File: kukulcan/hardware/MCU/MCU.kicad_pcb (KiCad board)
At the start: 4 copper layers, 78 x 53 mm, 88 parts, among them J1 Barrel_Jack_5V_In, J2 Barrel_Jack_5V_In, J3 USB_C_Receptacle, J4 SMA_GNSS, Q1 AO3401A, U1 TLV1117-33, U2 W25Q256JWEIQ, U3 ESP32-S3R16V, U4 BNO055, U5 NEO-M8N, U6 BMI088, U7 BME280, X1 40MHz, Y1 32.768kHz

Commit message: hw(mcu): update schematic and pcb
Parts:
- added svg2mod: G***, Core_System_2026:kukulcan, F.Cu at (163.5, 92.5)
- added svg2mod: G***, Core_System_2026:MarsRover, F.Cu at (141.2, 94.2)
- added svg2mod: G***, Core_System_2026:IMU_Axes_XYZ, F.Cu at (122.8, 87.2)
- FID1, FID2, FID3, FID4, FID5, FID6: footprint Fiducial:Fiducial_Cross_1.5mm_Mask2mm -> Fiducial:Fiducial_1mm_Mask3mm
- J4: footprint Connector_Coaxial:U.FL_Molex_MCRF_73412-0110_Vertical -> Connector_Coaxial:SMA_Amphenol_132134-10_Vertical
- U2: value W25Q256JWEIQ -> W25Q256JVEIQ; footprint Core_System_2026:W25Q256JWEIQ -> Core_System_2026:W25Q256JVEIQ
- U3: value ESP32-S3R16V -> ESP32-S3R8; footprint Core_System_2026:ESP32-S3R16V -> Core_System_2026:ESP32-S3R8
- moved FID6 59.0 mm to (125.8, 127.0)
- moved FID4 58.5 mm to (184.2, 82.0)
- moved FID5 45.0 mm to (184.2, 127.0)
- moved C29 4.25 mm to (125.5, 84.7), turned to 180 degrees
- moved J4 4.12 mm to (122.0, 119.0), turned to 90 degrees
- moved C28 3.55 mm to (125.8, 90.2), turned to 180 degrees
- moved C32 2.26 mm to (120.2, 111.8), turned to 180 degrees
- moved L3 1.68 mm to (119.2, 109.2), turned to -90 degrees
- moved U6 1.13 mm to (126.2, 87.5), turned to 180 degrees
- moved R14 0.79 mm to (120.2, 106.8)
- moved FID1 0.75 mm to (125.8, 81.2)
- moved FID3 0.50 mm to (184.2, 127.0)
- moved NxtPg1 0.25 mm to (150.0, 86.0)
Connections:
- net Net-(J4-In) renamed /RF_IN
- net Net-(L3-Pad1) renamed /RF2
- net Net-(U5-VCC_RF) renamed /RF1
- C5 pad 1: +VDD_SPI -> +3V3
- C6 pad 1: +VDD_SPI -> +3V3
- J3 pad S1: (no net) -> GND
- U2 pad 8: +VDD_SPI -> +3V3
- U3 pad 29: +VDD_SPI -> +3V3
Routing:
- net /RF_IN: track 0.00 -> 13.6 mm
- net +3V3: track 61.9 -> 71.5 mm, vias 48 -> 47
- net +VDD_SPI: track 9.01 -> 0.00 mm
- net SDA: track 74.3 -> 67.1 mm
- net GND: track 167.8 -> 174.0 mm, vias 124 -> 246
- net SCL: track 88.6 -> 94.2 mm
- net /RF1: track 0.00 -> 2.97 mm
- net NxtPg: track 16.4 -> 18.9 mm
- net /RF2: track 0.00 -> 1.66 mm
- net LED_WHITE: track 40.0 -> 41.0 mm
- net LedStrip: track 40.1 -> 40.9 mm
- net +VUSB: track 11.8 -> 12.4 mm
- removed copper zone on B.Cu, net +3V3
- removed copper zone on F.Cu, net +3V3
- removed copper zone on B.Cu, net +RB_VDD_5V
- removed copper zone on F.Cu, net +RB_VDD_5V
- removed copper zone on B.Cu, net +VDD_5V
- removed copper zone on F.Cu, net +VDD_5V
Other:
- board text added: "REV A RR 0126"

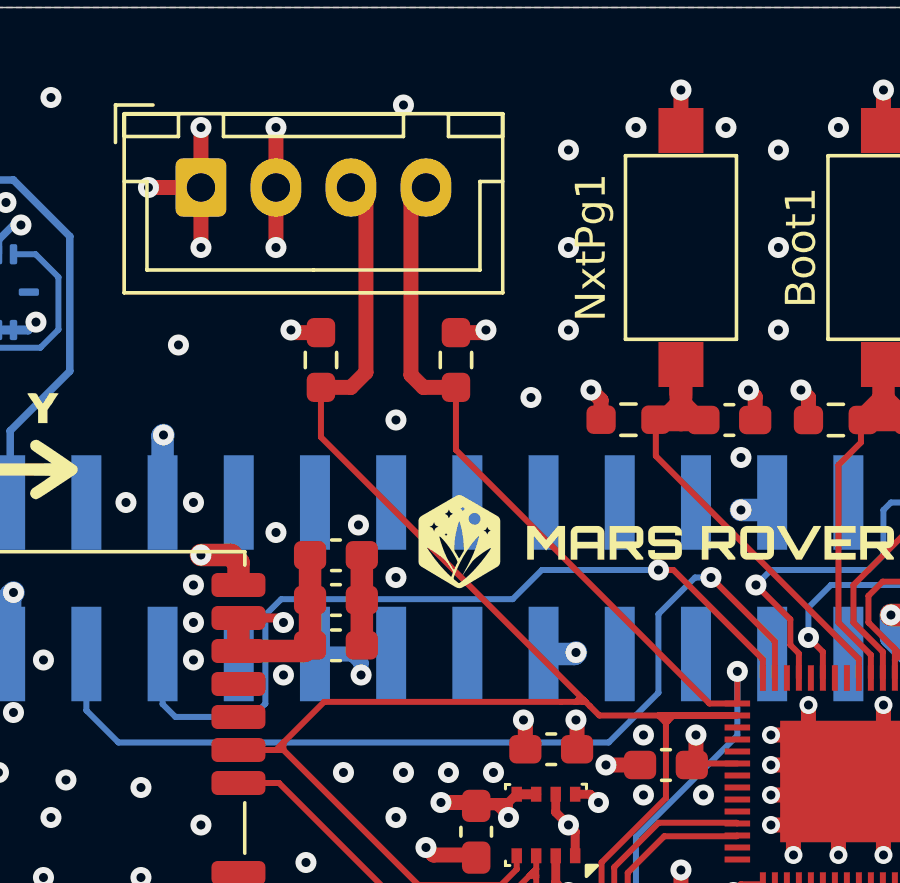
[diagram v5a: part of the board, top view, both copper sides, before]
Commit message: fix(kukulcan): I2C impedance change design error fix
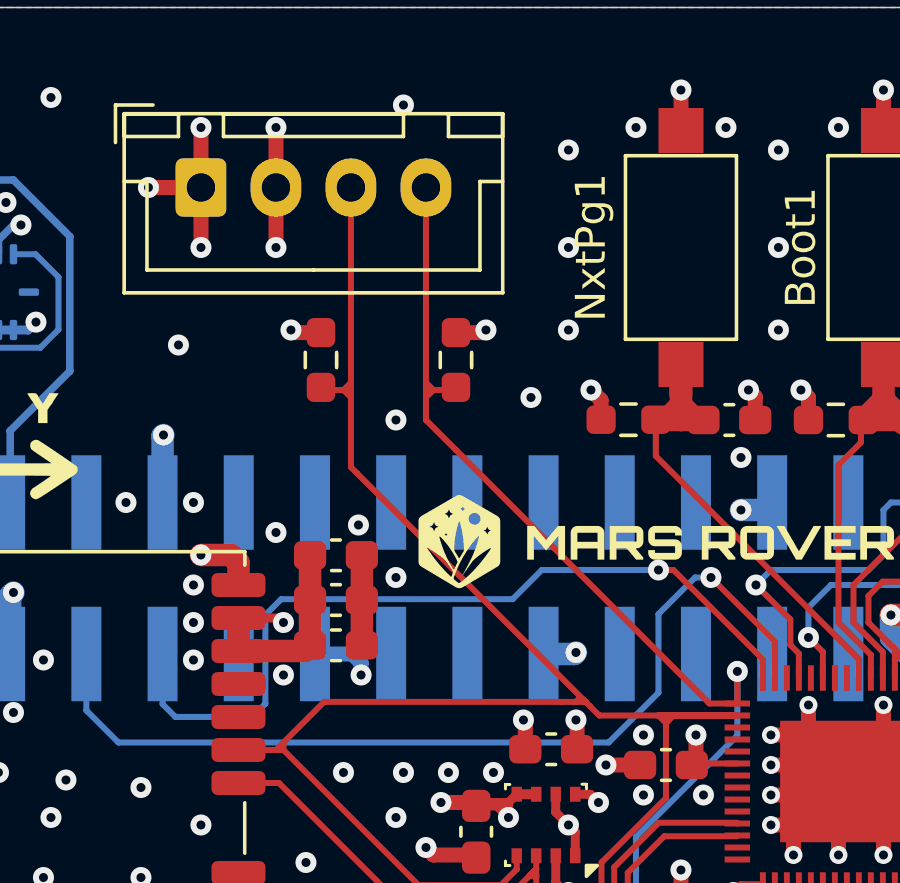
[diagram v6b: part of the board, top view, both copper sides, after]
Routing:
- net SDA: track 67.1 -> 67.8 mm
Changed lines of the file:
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@@
+	)
+	(segment
+		(start 139 90.5)
+		(end 139 84)
+		(width 0.2)
+		(layer "F.Cu")
+		(net 49)
 	)
 	(segment
@@
 	)
 	(segment
+		(start 139 90.75)
+		(end 139 90.5)
+		(width 0.2)
+		(layer "F.Cu")
+		(net 49)
+	)
+	(segment
 		(start 136.75 102.75)
 		(end 141.25 107.25)
@@
 	)
 	(segment
-		(start 138 92.322128)
-		(end 138 90.6625)
-		(width 0.2)
-		(layer "F.Cu")
-		(net 49)
-	)
-	(segment
-		(start 138 90.6625)
-		(end 139 90.6625)
-		(width 0.5)
+		(start 139 91)
+		(end 139 90.75)
+		(width 0.2)
 		(layer "F.Cu")
 		(net 49)
@@
 	)
 	(segment
+		(start 138.75 90.75)
+		(end 139 90.5)
+		(width 0.2)
+		(layer "F.Cu")
+		(net 49)
+	)
+	(segment
 		(start 146.752746 101.147)
 		(end 146.752746 101.074874)
@@
 	)
 	(segment
-		(start 139.5 90.1625)
-		(end 139.5 84.5)
-		(width 0.5)
-		(layer "F.Cu")
-		(net 49)
-	)
-	(segment
 		(start 141.775 114)
 		(end 142.5 114)
@@
 	)
 	(segment
+		(start 138.75 90.75)
+		(end 138.0875 90.75)
+		(width 0.2)
+		(layer "F.Cu")
+		(net 49)
+	)
+	(segment
+		(start 139 93.322128)
+		(end 139 91)
+		(width 0.2)
+		(layer "F.Cu")
+		(net 49)
+	)
+	(segment
+		(start 139 90.75)
+		(end 138.75 90.75)
+		(width 0.2)
+		(layer "F.Cu")
+		(net 49)
+	)
+	(segment
 		(start 149.5 102)
 		(end 149.5 101.85)
@@
 	(segment
 		(start 146.752746 101.074874)
-		(end 138 92.322128)
-		(width 0.2)
-		(layer "F.Cu")
-		(net 49)
-	)
-	(segment
-		(start 139.5 84.5)
-		(end 139 84)
-		(width 0.5)
+		(end 139.213936 93.536064)
+		(width 0.2)
 		(layer "F.Cu")
 		(net 49)
@@
 	)
 	(segment
+		(start 139.213936 93.536064)
+		(end 139 93.322128)
+		(width 0.2)
+		(layer "F.Cu")
+		(net 49)
+	)
+	(segment
 		(start 149.644 101.6)
 		(end 149.75 101.6)
@@
 	)
 	(segment
+		(start 138.0875 90.75)
+		(end 138 90.6625)
+		(width 0.2)
+		(layer "F.Cu")
+		(net 49)
+	)
+	(segment
 		(start 149.5 102)
 		(end 149.5 101.6)
@@
 	)
 	(segment
-		(start 139 90.6625)
-		(end 139.5 90.1625)
-		(width 0.5)
-		(layer "F.Cu")
-		(net 49)
-	)
-	(segment
 		(start 141.25 107.25)
 		(end 144 107.25)
@@
 		(start 146.752746 101.147)
 		(end 146.5 101.147)
+		(width 0.2)
+		(layer "F.Cu")
+		(net 49)
+	)
+	(segment
+		(start 139 91)
+		(end 138.75 90.75)
 		(width 0.2)
 		(layer "F.Cu")
@@
 	)
 	(segment
+		(start 141.5 91)
+		(end 141.5 90.75)
+		(width 0.2)
+		(layer "F.Cu")
+		(net 76)
+	)
+	(segment
 		(start 145.175 108)
 		(end 145.175 107)
@@
 	)
 	(segment
-		(start 142.5 92.75)
-		(end 142.5 90.6625)
+		(start 141.75 90.75)
+		(end 141.5 90.5)
+		(width 0.2)
+		(layer "F.Cu")
+		(net 76)
+	)
+	(segment
+		(start 141.5 90.75)
+		(end 141.75 90.75)
 		(width 0.2)
 		(layer "F.Cu")
@@
 	)
 	(segment
+		(start 142.4125 90.75)
+		(end 142.5 90.6625)
+		(width 0.2)
+		(layer "F.Cu")
+		(net 76)
+	)
+	(segment
 		(start 142.265271 113.0875)
 		(end 145.175 110.177771)
@@
 	)
 	(segment
-		(start 141 90.25)
-		(end 141 84.5)
-		(width 0.5)
-		(layer "F.Cu")
-		(net 76)
-	)
-	(segment
 		(start 145.175 108.575)
 		(end 145.25 108.5)
@@
 	)
 	(segment
+		(start 141.75 90.75)
+		(end 142.4125 90.75)
+		(width 0.2)
+		(layer "F.Cu")
+		(net 76)
+	)
+	(segment
+		(start 141.5 90.5)
+		(end 141.5 84)
+		(width 0.2)
+		(layer "F.Cu")
+		(net 76)
+	)
+	(segment
+		(start 141.5 91.75)
+		(end 141.5 91)
+		(width 0.2)
+		(layer "F.Cu")
+		(net 76)
+	)
+	(segment
+		(start 142.5 92.75)
+		(end 141.5 91.75)
+		(width 0.2)
+		(layer "F.Cu")
+		(net 76)
+	)
+	(segment
 		(start 145.175 109)
 		(end 145.175 108.575)
@@
 	)
 	(segment
-		(start 141.4125 90.6625)
-		(end 141 90.25)
-		(width 0.5)
-		(layer "F.Cu")
-		(net 76)
-	)
-	(segment
 		(start 145.175 108)
 		(end 145.175 108.425)
@@
 	)
 	(segment
-		(start 141 84.5)
-		(end 141.5 84)
-		(width 0.5)
-		(layer "F.Cu")
-		(net 76)
-	)
-	(segment
 		(start 136.6 103.85)
 		(end 135.25 103.85)
@@
 	)
 	(segment
-		(start 142.5 90.6625)
-		(end 141.4125 90.6625)
-		(width 0.5)
-		(layer "F.Cu")
-		(net 76)
-	)
-	(segment
 		(start 151.88 101.2)
 		(end 151.88 100.13)
@@
 		(width 0.2)
 		(layer "F.Cu")
+		(net 76)
+	)
+	(segment
+		(start 141.5 91)
+		(end 141.75 90.75)
+		(width 0.2)
+		(layer "F.Cu")
+		(net 76)
+	)
+	(segment
+		(start 141.5 90.75)
+		(end 141.5 90.5)
+		(width 0.2)
+		(layer "F.Cu")
